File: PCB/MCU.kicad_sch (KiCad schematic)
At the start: 12 parts, among them J1 Conn_02x15_Counter_Clockwise, J7 Conn_ARM_JTAG_SWD_10, U11 STM32H743VITx

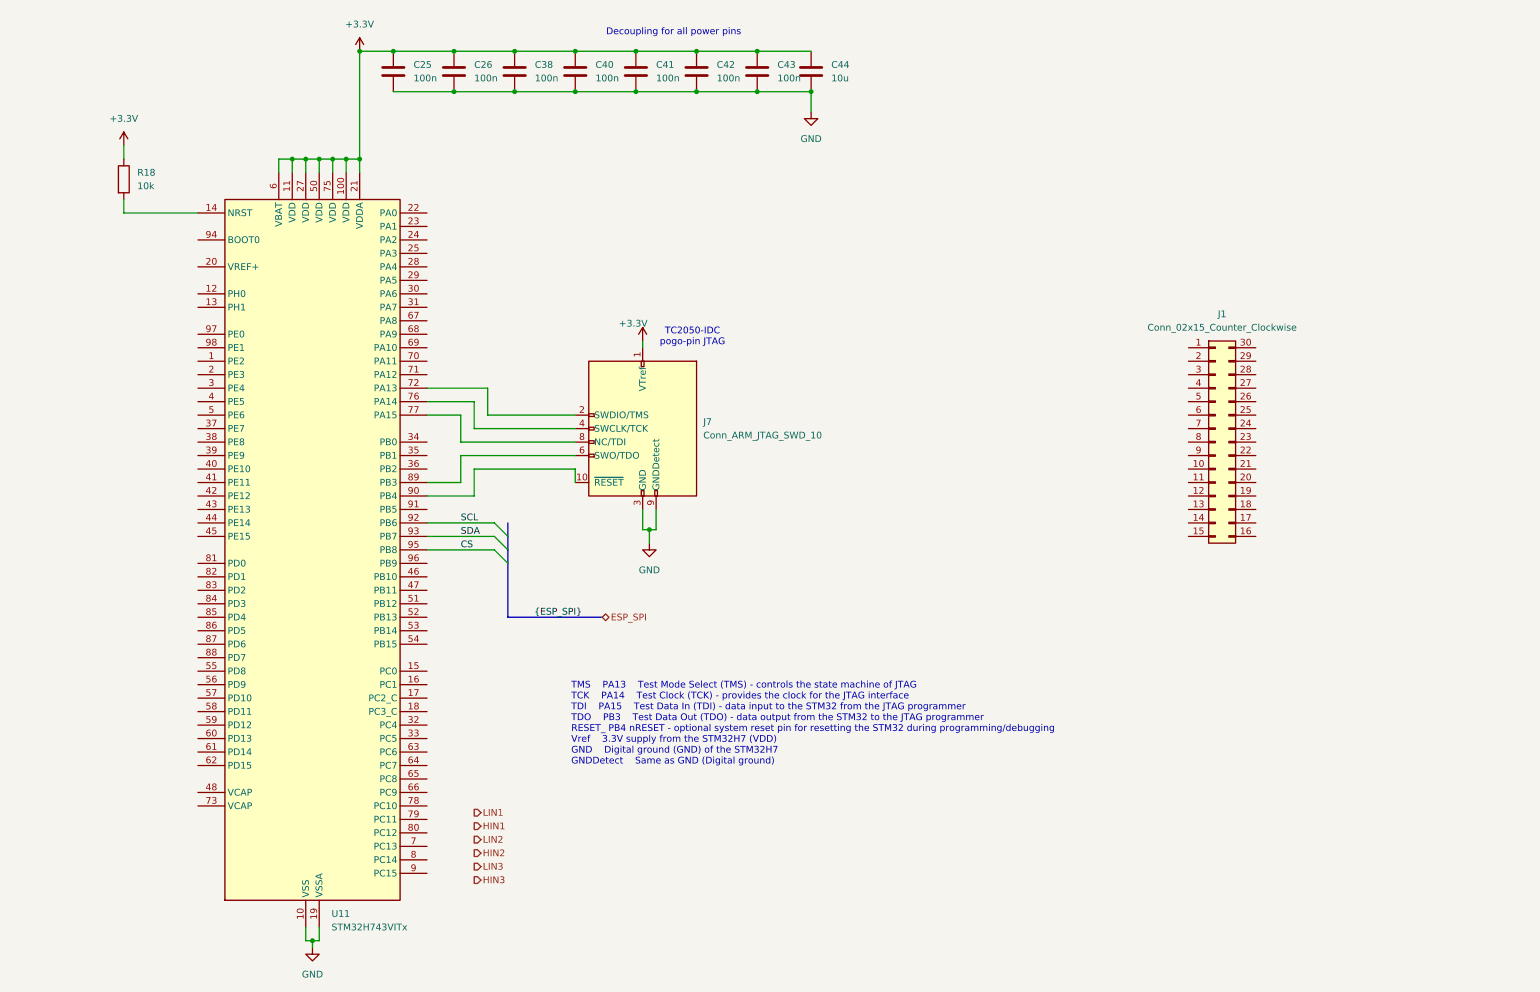
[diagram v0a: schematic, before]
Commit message: Hardware updates: STM32H7 and Inverted design
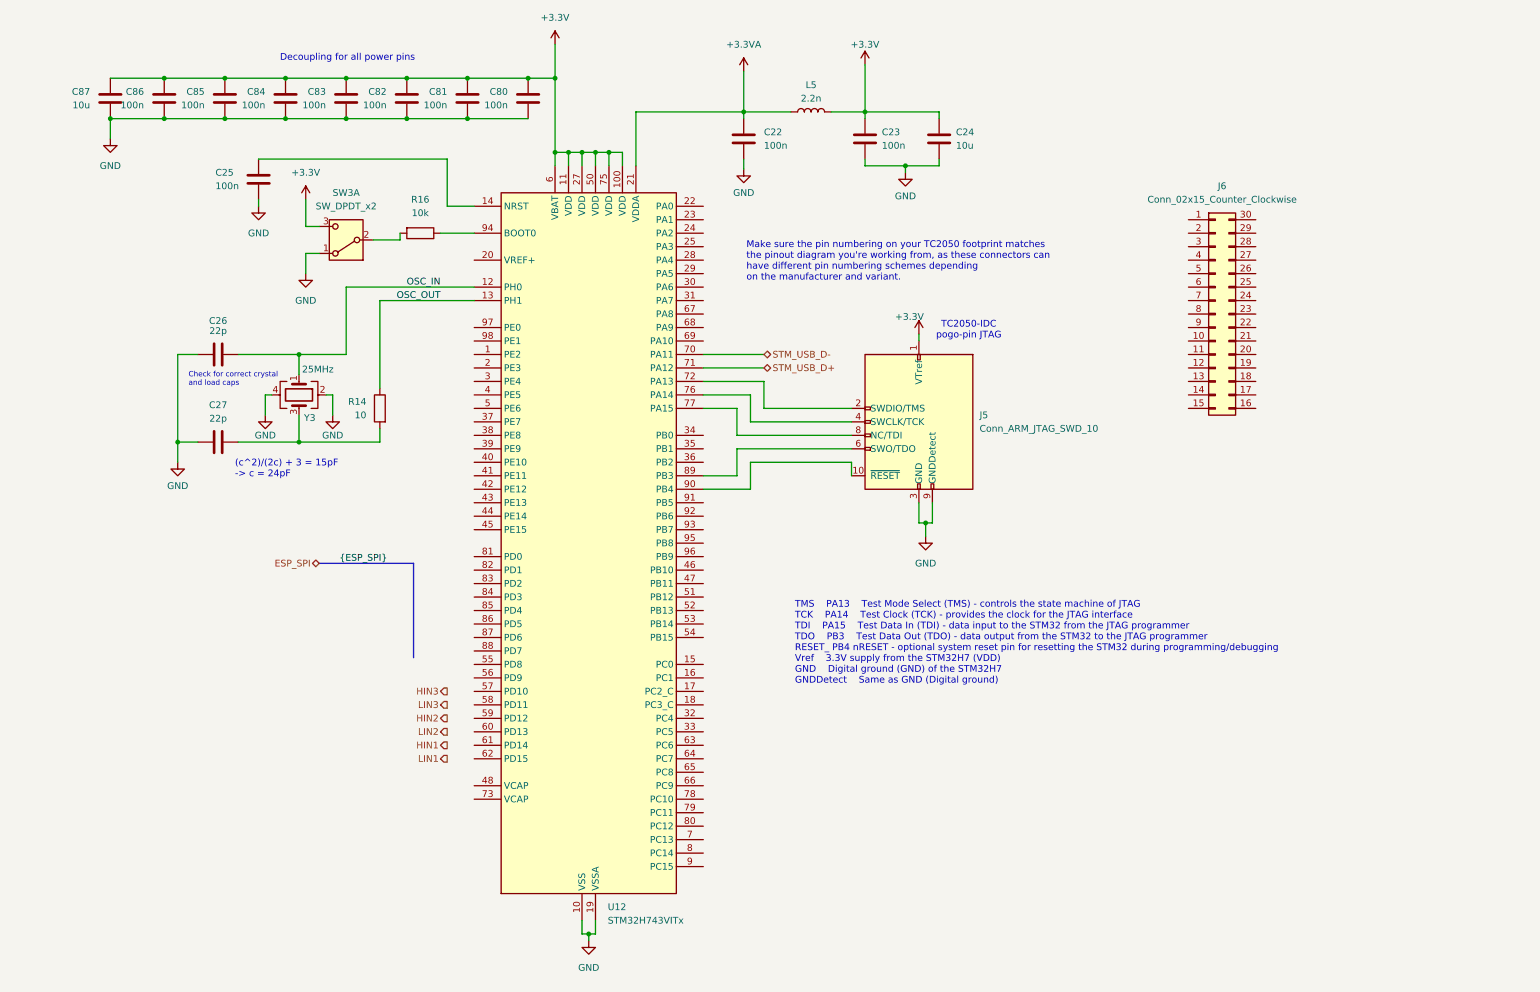
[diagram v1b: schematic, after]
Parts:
- removed R18: 10k, Resistor_SMD:R_0603_1608Metric, symbol Device:R
- added C22, C23: 100n, Capacitor_SMD:C_0402_1005Metric, symbol Device:C
- added C24: 10u, Capacitor_SMD:C_0603_1608Metric, symbol Device:C
- added C25: 100n, Resistor_SMD:R_0402_1005Metric, symbol Device:C
- added C26, C27: 22p, Capacitor_SMD:C_0402_1005Metric, symbol Device:C
- added L5: 2.2n, Inductor_SMD:L_0402_1005Metric, symbol Device:L
- added R14: 10, Resistor_SMD:R_0402_1005Metric, symbol Device:R
- added R16: 10k, Resistor_SMD:R_0402_1005Metric, symbol Device:R
- added SW3: SW_DPDT_x2, symbol Switch:SW_DPDT_x2
- added Y3: 25MHz, Crystal:Crystal_SMD_3225-4Pin_3.2x2.5mm, symbol Device:Crystal_GND24
- renumbered C25 to C80, C26 to C81, C38 to C82, C40 to C83, C41 to C84, C42 to C85, C43 to C86, C44 to C87, J7 to J5, J1 to J6, U11 to U12
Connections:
- net +3.3V: now also C23.1, C24.1, L5.2, SW3.3 (C); no longer U12.21 (VDDA)
- net GND: now also C22.2, C23.2, C24.2, C25.2, C26.1, C27.1, SW3.1 (A), Y3.2, Y3.4
- net at U12.14 (NRST): now also C25.1
- net OSC_IN: now reaches U12.12 (PH0)
- net OSC_IN: now also C26.2, Y3.1
- net OSC_OUT: now reaches U12.13 (PH1)
- net OSC_OUT: now also R14.1
- net STM_USB_D-: now reaches U12.70 (PA11)
- net STM_USB_D+: now reaches U12.71 (PA12)
- net at U12.94 (BOOT0): now also R16.1
- net CS: no longer names the net of U12.95 (PB8)
- net SCL: no longer names the net of U12.92 (PB6)
- net SDA: no longer names the net of U12.93 (PB7)
- new net: C27.2, R14.2, Y3.3
- new net: R16.2, SW3.2 (B)
- new net +3.3VA: C22.1, L5.1, U12.21 (VDDA)
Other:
- note added: "(c^2)/(2c) + 3 = 15pF -> c = 24pF"
- note added: "Check for correct crystal and load caps"
- note added: "Make sure the pin numbering on your TC2050 footprint matches the pinout diagram you're working from, as these connectors can have different pin numbering schemes depending on the manufacturer and variant."
- moved on the sheet: C80, C81, C82, C83, C84, C85, C86, C87, J5, J6, U12

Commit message: Latest PCB version
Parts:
- removed J5: Conn_ARM_JTAG_SWD_10, Connector:Tag-Connect_TC2050-IDC-FP_2x05_P1.27mm_Vertical, symbol Connector:Conn_ARM_JTAG_SWD_10
- removed J6: Conn_02x15_Counter_Clockwise, Connector_PinHeader_2.54mm:PinHeader_2x15_P2.54mm_Horizontal, symbol Connector_Generic:Conn_02x15_Counter_Clockwise
- added C88, C89: 2.2u, Capacitor_SMD:C_0603_1608Metric, symbol Device:C
- added D11, D12, D13, D6, D7: SZESD9B5.0ST5G, Diode_SMD:D_SOD-923, symbol Diode:SZESD9B5.0ST5G
- added D5: LED, LED_SMD:LED_0805_2012Metric_Pad1.15x1.40mm_HandSolder, symbol Device:LED_Small
- added J6: TC2030, Connector:Tag-Connect_TC2030-IDC-FP_2x03_P1.27mm_Vertical, symbol Connector:Conn_ARM_SWD_TagConnect_TC2030
- added J7, J8: Conn_01x04, Connector_PinHeader_2.54mm:PinHeader_1x04_P2.54mm_Horizontal, symbol Connector_Generic:Conn_01x04
- added J9: Conn_02x10_Counter_Clockwise, Connector_PinHeader_2.54mm:PinHeader_2x11_P2.54mm_Vertical, symbol Connector_Generic:Conn_02x10_Counter_Clockwise
- added R27: 1k, Resistor_SMD:R_0402_1005Metric, symbol Device:R_Small
- SW3: footprint (none) -> Button_Switch_SMD:SW_SPDT_PCM12
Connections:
- net +3.3V: now also D6.2 (A2), J6.1 (VCC)
- net GND: now also C88.2, C89.2, D11.1 (A1), D12.1 (A1), D13.1 (A1), D6.1 (A1), D7.1 (A1), J6.5 (GND), R27.2
- net HIN1: now also U12.85 (PD4)
- net HIN2: now also U12.83 (PD2)
- net HIN3: now also U12.81 (PD0)
- net LIN1: now also U12.86 (PD5)
- net LIN2: now also U12.84 (PD3)
- net LIN3: now also U12.82 (PD1)
- net SWDIO: now reaches U12.72 (PA13)
- net SWDIO: now also D12.2 (A2), J6.2 (SWDIO)
- net SWCLK: now reaches U12.76 (PA14)
- net SWCLK: now also D11.2 (A2), J6.4 (SWCLK)
- net SWO/TDO: now reaches U12.89 (PB3)
- net SWO/TDO: now also D13.2 (A2), J6.6 (SWO)
- net NRST: now reaches C25.1, U12.14 (NRST)
- net NRST: now also D7.2 (A2), J6.3 (~{RESET})
- net CS: now reaches U12.28 (PA4)
- net SCLK: now reaches U12.29 (PA5)
- net MISO: now reaches U12.30 (PA6)
- net MOSI: now reaches U12.31 (PA7)
- net at U12.48 (VCAP): now also C88.1
- net at U12.68 (PA9): now also D5.2 (A)
- net at U12.73 (VCAP): now also C89.1
- new net: D5.1 (K), R27.1
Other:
- note added: "Boot Opt"
- note added: "Low ESR!"
- note added: "Make sure the pin numbering on TC2030 footprint matches the pinout diagram you're working from, as these connectors can have different pin numbering schemes depending on the manufacturer and variant."
- note added: "Maybe add push button to NRST"
- note added: "TC2030 pogo-pin debug and programming adapter consider adding 22 Ohm series resistors"
- note removed: "Make sure the pin numbering on your TC2050 footprint matches the pinout diagram you're working from, as these connectors can have different pin numbering schemes depending on the manufacturer and variant."
- note removed: "TC2050-IDC pogo-pin JTAG"
- moved on the sheet: C23, C24, C25, R14, SW3A
